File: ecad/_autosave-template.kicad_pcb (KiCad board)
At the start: 2 copper layers, 25.2 x 27.3 mm, 12 parts, among them P1 CF_EXP_LEFT, P2 CF_EXP_RIGHT, P3 CONN_2, P4 CONN_2, Q1 DMG2302U, Q2 DMG2302U

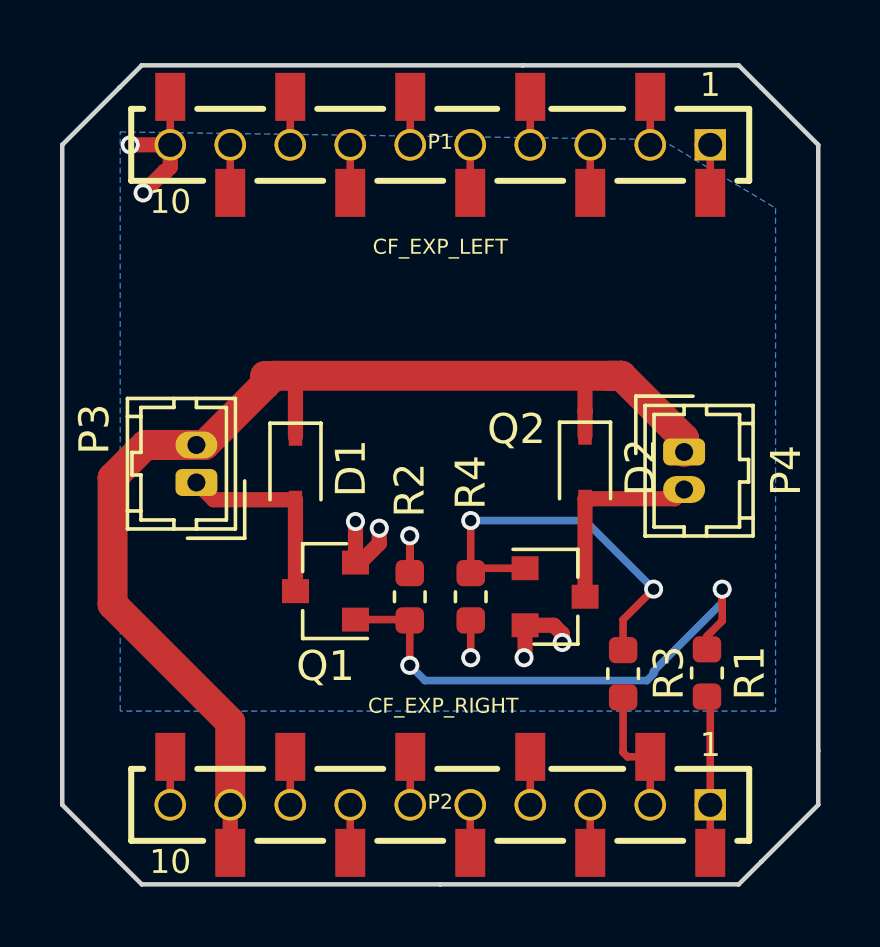
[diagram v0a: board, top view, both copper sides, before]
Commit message: modified schematic and pcb layout + plotted production files
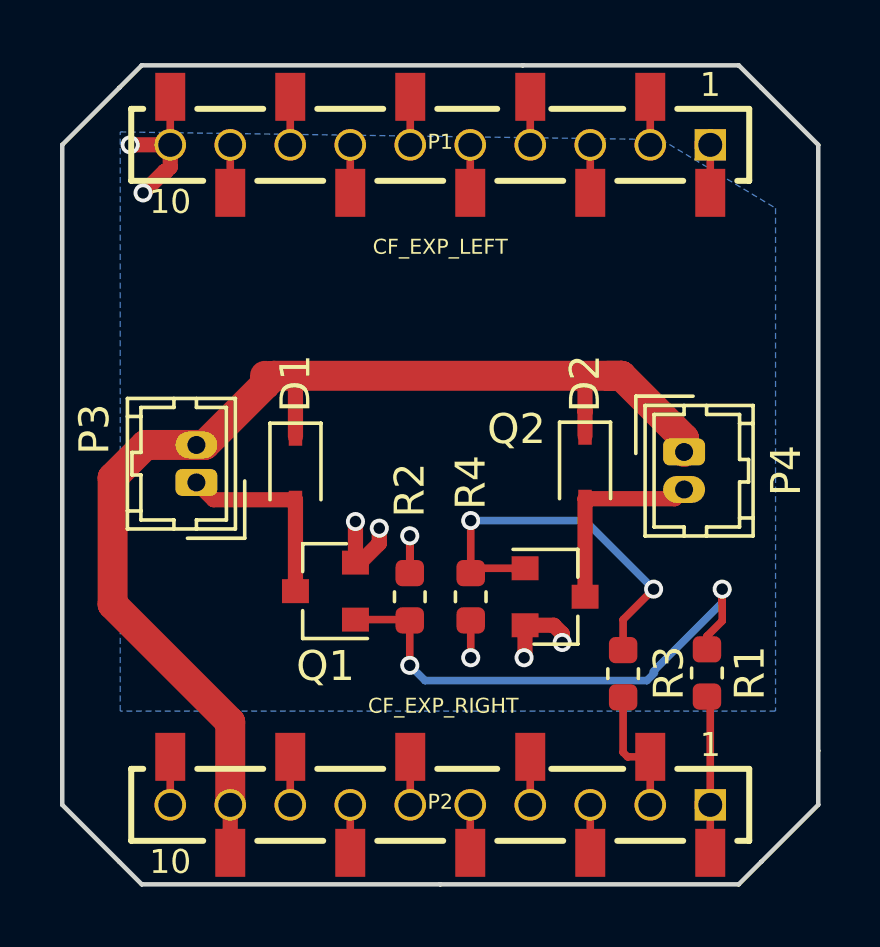
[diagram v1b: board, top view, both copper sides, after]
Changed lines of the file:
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@@
     (32 B.Adhes user hide)
     (33 F.Adhes user hide)
-    (34 B.Paste user)
-    (35 F.Paste user)
-    (36 B.SilkS user)
+    (34 B.Paste user hide)
+    (35 F.Paste user hide)
+    (36 B.SilkS user hide)
     (37 F.SilkS user)
-    (38 B.Mask user)
-    (39 F.Mask user)
-    (40 Dwgs.User user)
+    (38 B.Mask user hide)
+    (39 F.Mask user hide)
+    (40 Dwgs.User user hide)
     (42 Eco1.User user hide)
-    (43 Eco2.User user)
+    (43 Eco2.User user hide)
     (44 Edge.Cuts user)
   )
@@
     (visible_elements 7FFFFFFF)
     (pcbplotparams
-      (layerselection 0x010f8_80000001)
+      (layerselection 0x010f0_ffffffff)
       (usegerberextensions true)
       (usegerberattributes false)
@@
       (excludeedgelayer true)
       (linewidth 0.150000)
-      (plotframeref true)
+      (plotframeref false)
       (viasonmask false)
       (mode 1)
@@
       (psnegative false)
       (psa4output false)
-      (plotreference false)
+      (plotreference true)
       (plotvalue false)
       (plotinvisibletext false)
@@
     (tags SOD-323)
     (attr smd)
-    (fp_text reference D1 (at 0 -1.85 90) (layer F.SilkS)
+    (fp_text reference D1 (at -2.828 0 90) (layer F.SilkS)
       (effects (font (size 1 1) (thickness 0.15)))
     )
@@
     (tags SOD-323)
     (attr smd)
-    (fp_text reference D2 (at 0 -1.85 90) (layer F.SilkS)
+    (fp_text reference D2 (at -2.794 0 90) (layer F.SilkS)
       (effects (font (size 1 1) (thickness 0.15)))
     )
